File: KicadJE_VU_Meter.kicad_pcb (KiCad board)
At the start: 2 copper layers, 242 x 128 mm, 39 parts

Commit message: Update KicadJE_VU_Meter.kicad_pcb
Routed
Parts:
- removed G*** (x3): LOGO, AJ:Johansen_engineering_logo_20mm
- removed H101 (x2), H301: ON, AJ:LED_Hole_3mm
- removed H102 (x2), H103 (x2), H104, H105: MountingHole_Pad, AJ:MountingHole_Eurorack3
- removed TP102 (x2), TP303: SQ, AJ:Jack_6m3
- removed TP103 (x2), TP301: In1, AJ:Jack_6m3
- removed TP105 (x2): In3, AJ:Jack_6m3
- removed TP106 (x2): HS, AJ:Jack_6m3
- removed TP107 (x3): OFF1, AJ:Pot_6m3_scale1
- removed TP107 (x2): FM, AJ:Jack_6m3
- removed TP108 (x2): PWM, AJ:Jack_6m3
- removed TP112 (x3): Fine, AJ:Pot_6m3_scale1
- removed TP302: Tri, AJ:Jack_6m3
- removed TP304: PWM1, AJ:Pot_6m3_scale1
- removed TP305: PWM2, AJ:Pot_6m3_scale1
- added C1: 1u, Capacitor_SMD:C_0805_2012Metric, B.Cu at (136.9, 44.0)
- added C2: 1u, Capacitor_SMD:C_0805_2012Metric, B.Cu at (103.0, 45.0)
- added C4: 100n, Capacitor_SMD:C_0805_2012Metric, B.Cu at (124.5, 108.5)
- added C5: 100n, Capacitor_SMD:C_0805_2012Metric, B.Cu at (134.0, 115.5)
- added C7: 100n, Capacitor_SMD:C_0805_2012Metric, B.Cu at (130.3, 120.0)
- added C8: 220p, Capacitor_SMD:C_0805_2012Metric, B.Cu at (133.9, 118.0)
- added C9: 1u-22u, Capacitor_SMD:C_1206_3216Metric, B.Cu at (129.0, 97.0)
- added D1: 1N1007, Diode_SMD:D_SOD-123, B.Cu at (132.0, 44.0)
- added D10: 1N4148, Diode_SMD:D_MiniMELF, B.Cu at (121.5, 103.0)
- added D11: 1N4148, Diode_SMD:D_MiniMELF, B.Cu at (121.5, 97.2)
- added D2: 1N1007, Diode_SMD:D_SOD-123, B.Cu at (108.0, 45.0)
- added D3: LED, LED_SMD:LED_0805_2012Metric_Pad1.15x1.40mm_HandSolder, F.Cu at (120.4, 45.7)
- added D4: 1N1007, Diode_SMD:D_SOD-123, B.Cu at (116.5, 112.5)
- added D5: 1N1007, Diode_SMD:D_SOD-123, B.Cu at (116.5, 127.5)
- added D6: 1N1007, Diode_SMD:D_SOD-123, B.Cu at (116.5, 117.5)
- added D7: 1N1007, Diode_SMD:D_SOD-123, B.Cu at (116.5, 122.5)
- added D8: 1N4148, Diode_SMD:D_MiniMELF, B.Cu at (117.5, 103.0)
- added D9: 1N4148, Diode_SMD:D_MiniMELF, B.Cu at (117.5, 97.2)
- added H5: Meter, AJ:VU_Meter_Hole, F.Cu at (120.4, 68.6)
- added H6: Jack, AJ:Jack_6m3, F.Cu at (131.0, 145.0)
- added H7: Jack, AJ:Jack_3m5, F.Cu at (110.0, 115.0)
- added H8: Jack, AJ:Jack_3m5, F.Cu at (110.0, 125.0)
- added H9: Jack, AJ:Jack_3m5, F.Cu at (110.0, 145.0)
- added J1: Out, Connector_PinHeader_2.54mm:PinHeader_1x03_P2.54mm_Vertical_SMD_Pin1Right, B.Cu at (110.0, 153.0)
- added J2: In1, Connector_PinHeader_2.54mm:PinHeader_1x03_P2.54mm_Vertical_SMD_Pin1Right, B.Cu at (110.0, 106.0)
- added J3: In2, Connector_PinHeader_2.54mm:PinHeader_1x03_P2.54mm_Vertical_SMD_Pin1Right, B.Cu at (110.0, 134.0)
- added J4: Out, Connector_PinHeader_2.54mm:PinHeader_1x03_P2.54mm_Vertical_SMD_Pin1Right, B.Cu at (133.0, 134.0)
- added MES1: VU Meter, Connector_PinHeader_2.54mm:PinHeader_1x02_P2.54mm_Vertical_SMD_Pin1Right, B.Cu at (134.0, 97.0)
- added MES2: VU Meter Backlight, Connector_PinHeader_2.54mm:PinHeader_1x02_P2.54mm_Vertical_SMD_Pin1Right, B.Cu at (110.0, 97.0)
- added P1: HEADER_2x5_Doepfer, Connector_PinHeader_2.54mm:PinHeader_2x05_P2.54mm_Vertical_SMD, B.Cu at (121.0, 45.0)
- added R1: 22k, Resistor_SMD:R_0805_2012Metric_Pad1.20x1.40mm_HandSolder, B.Cu at (132.0, 46.5)
- added R11: 100k, Resistor_SMD:R_0805_2012Metric_Pad1.20x1.40mm_HandSolder, B.Cu at (120.5, 110.5)
- added R12: 100k, Resistor_SMD:R_0805_2012Metric_Pad1.20x1.40mm_HandSolder, B.Cu at (120.5, 113.0)
- added R13: 100k, Resistor_SMD:R_0805_2012Metric_Pad1.20x1.40mm_HandSolder, B.Cu at (126.2, 122.2)
- added R14: OPEN, Resistor_SMD:R_0805_2012Metric_Pad1.20x1.40mm_HandSolder, B.Cu at (126.2, 120.0)
- added R15: OPEN, Resistor_SMD:R_0805_2012Metric_Pad1.20x1.40mm_HandSolder, B.Cu at (120.5, 115.5)
- added R16: 100k, Resistor_SMD:R_0805_2012Metric_Pad1.20x1.40mm_HandSolder, B.Cu at (128.0, 117.5)
- added R19: 1M, Resistor_SMD:R_0805_2012Metric_Pad1.20x1.40mm_HandSolder, B.Cu at (130.2, 122.2)
- added R2: OPEN, Resistor_SMD:R_0805_2012Metric_Pad1.20x1.40mm_HandSolder, B.Cu at (103.5, 150.5)
- added R20: 10k, Resistor_SMD:R_0805_2012Metric_Pad1.20x1.40mm_HandSolder, B.Cu at (128.0, 115.5)
- added R22: 10k, Resistor_SMD:R_0805_2012Metric_Pad1.20x1.40mm_HandSolder, B.Cu at (134.2, 122.2)
- added R23: 470R, Resistor_SMD:R_0805_2012Metric_Pad1.20x1.40mm_HandSolder, B.Cu at (130.2, 124.2)
- added R24: 1k, Resistor_SMD:R_0805_2012Metric_Pad1.20x1.40mm_HandSolder, B.Cu at (124.4, 113.0)
- added R26: 150, Resistor_SMD:R_0805_2012Metric_Pad1.20x1.40mm_HandSolder, B.Cu at (125.5, 98.5)
- added R27: 150, Resistor_SMD:R_0805_2012Metric_Pad1.20x1.40mm_HandSolder, B.Cu at (125.5, 95.5)
- added R28: OPEN, Resistor_SMD:R_0805_2012Metric_Pad1.20x1.40mm_HandSolder, B.Cu at (126.0, 136.0)
- added R29: 1k, Resistor_SMD:R_0805_2012Metric_Pad1.20x1.40mm_HandSolder, B.Cu at (126.0, 131.0)
- added R3: 10k, Resistor_SMD:R_0805_2012Metric_Pad1.20x1.40mm_HandSolder, B.Cu at (103.5, 101.5)
- added R4: 10k, Resistor_SMD:R_0805_2012Metric_Pad1.20x1.40mm_HandSolder, B.Cu at (103.5, 131.5)
- added R5: 1k, Resistor_SMD:R_0805_2012Metric_Pad1.20x1.40mm_HandSolder, B.Cu at (116.5, 150.5)
- added R7: 10k, Resistor_SMD:R_0805_2012Metric_Pad1.20x1.40mm_HandSolder, B.Cu at (116.5, 108.0)
- added R8: 10k, Resistor_SMD:R_0805_2012Metric_Pad1.20x1.40mm_HandSolder, B.Cu at (116.5, 132.0)
- added TP1: Out, TestPoint:TestPoint_Pad_D2.0mm, B.Cu at (102.0, 145.0)
- added TP2: In2, TestPoint:TestPoint_Pad_D2.0mm, B.Cu at (102.0, 125.0)
- added TP3: Flow1, TestPoint:TestPoint_Pad_D2.0mm, B.Cu at (121.8, 150.2)
- added TP4: Out, TestPoint:TestPoint_Pad_D2.0mm, B.Cu at (138.0, 140.0)
- added U1: TL072, Package_SO:SO-8_5.3x6.2mm_P1.27mm, B.Cu at (131.0, 110.5)
- moved H1 93.0 mm to (106.5, 39.0)
- moved H2 93.0 mm to (106.5, 161.0)
- moved H3 93.0 mm to (133.5, 39.0)
- moved H4 93.0 mm to (133.5, 161.0)
- renumbered H102 to H1, H103 to H2, H104 to H3, H105 to H4
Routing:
- net +12VA: track 0.00 -> 216.5 mm
- net -12VA: track 0.00 -> 209.0 mm, vias 0 -> 1
- net GND: track 0.00 -> 66.3 mm, vias 0 -> 6
- net Net-(C8-Pad2): track 0.00 -> 58.6 mm, vias 0 -> 2
- net Flow1: track 0.00 -> 56.0 mm
- net Net-(C8-Pad1): track 0.00 -> 39.5 mm
- net Net-(R22-Pad1): track 0.00 -> 30.3 mm
- net Net-(D5-Pad2): track 0.00 -> 19.9 mm
- net Net-(J3-Pad1): track 0.00 -> 18.3 mm
- net Net-(J1-Pad2): track 0.00 -> 16.4 mm
- net Net-(J1-Pad1): track 0.00 -> 15.8 mm
- net Net-(J4-Pad1): track 0.00 -> 15.7 mm
- net Net-(D3-Pad2): track 0.00 -> 14.1 mm, vias 0 -> 1
- net Net-(J4-Pad2): track 0.00 -> 13.3 mm
- net Net-(D10-Pad1): track 0.00 -> 11.5 mm
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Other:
- board size 242 x 128 mm -> 40 x 128 mm
- board text added: "Johansen Engineering VU Rev A 10/04-2021"
- board text added: "Out"
- board text added: "VU"
- board text removed: "CV"
- board text removed: "CV Util Rev A 22/03-2020 Johansen Engineering"
- board text removed: "CV1"
- board text removed: "CV2"
- board text removed: "GLIDE"
- board text removed: "Gain1"
- board text removed: "Gain2"
- board text removed: "Glide1"
- board text removed: "Glide2"
- board text removed: "IN"
- board text removed: "Inv1"
- board text removed: "Inv2"
- board text removed: "Johansen Engineering Glide Rev A 22/03-2020"
- board text removed: "Offset1"
- board text removed: "Offset2"
- board text removed: "Out1"
- board text removed: "Out2"
- board text removed: "Phase1"
- board text removed: "Phase2"
- board text removed: "SHIFT"
- board text removed: "TIME"
- board text removed: "TimeShift Rev A 22/03-2020 Johansen Engineering"

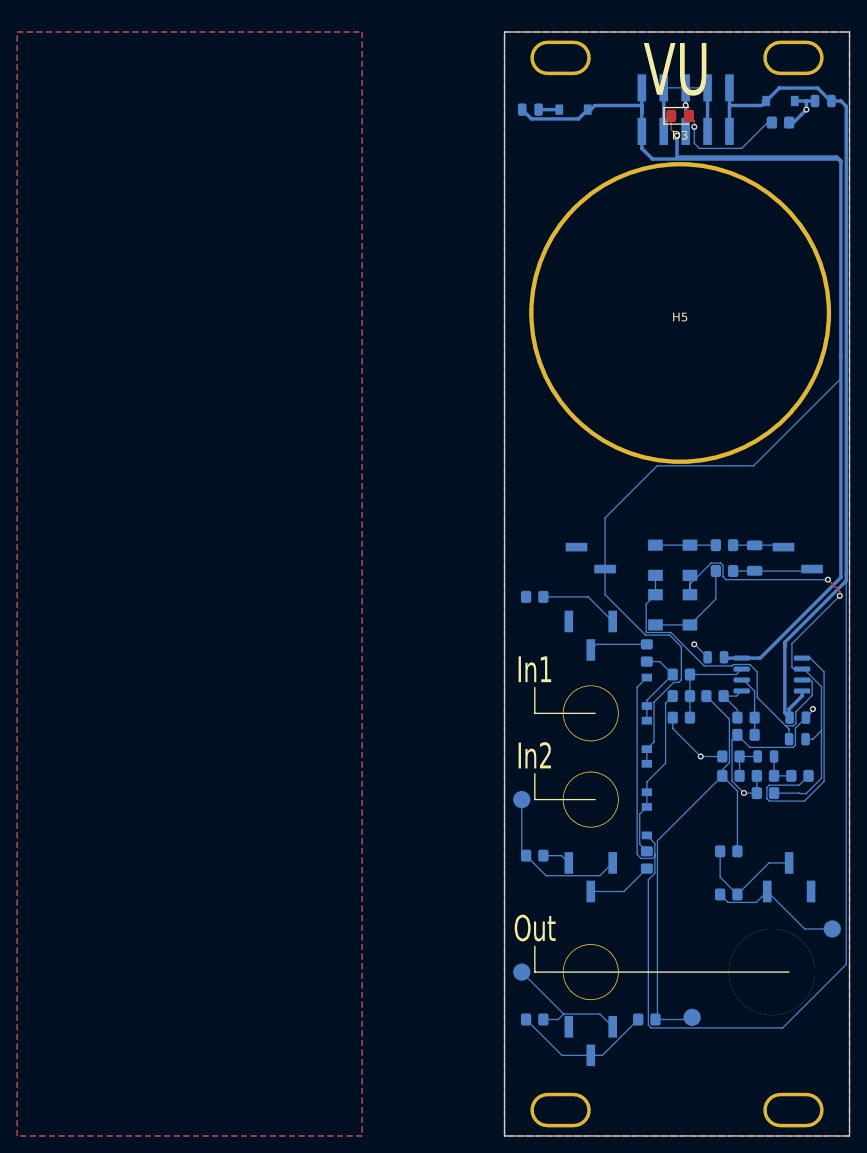
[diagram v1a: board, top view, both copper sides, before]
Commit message: Reposition VU meter
To make sure there is room for the power conn.
2mm available for jacks
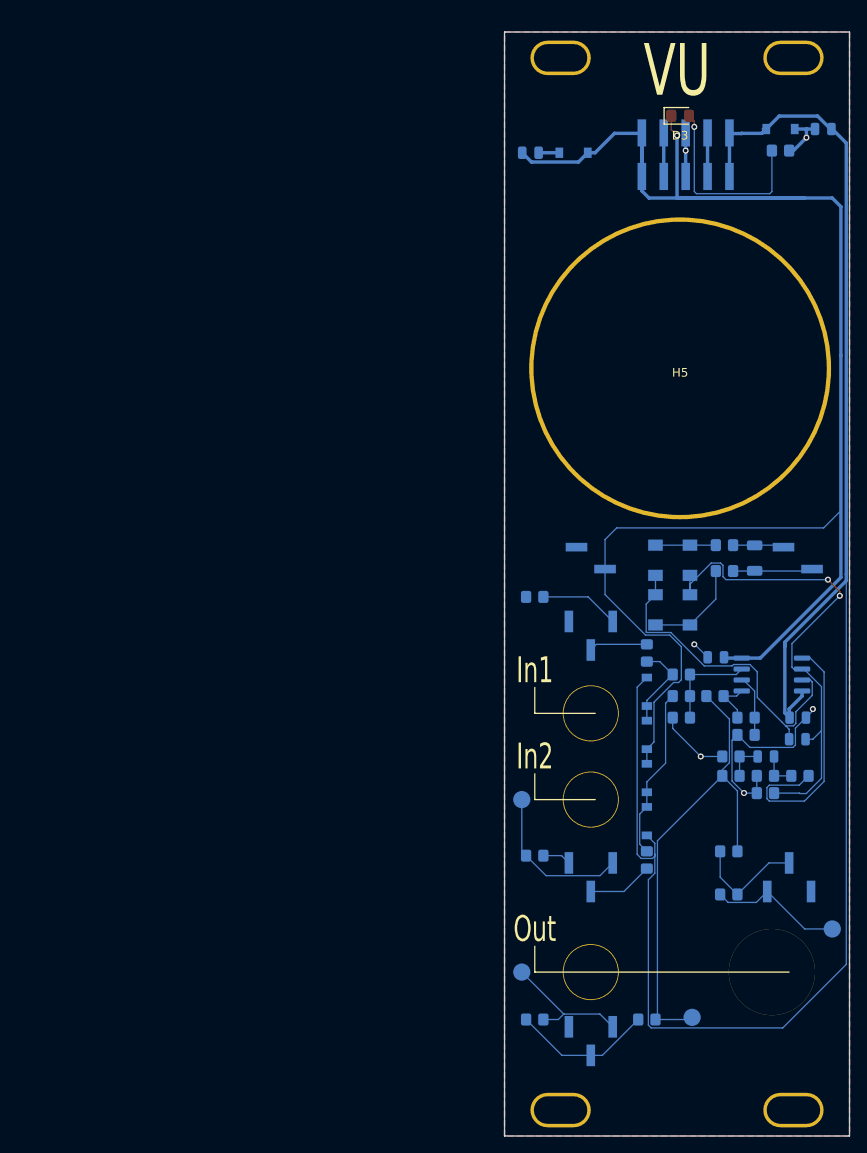
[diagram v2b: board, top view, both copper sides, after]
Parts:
- moved H5 6.42 mm to (120.4, 75.0)
- moved P1 5.23 mm to (121.0, 50.2)
- moved C2 5.00 mm to (103.0, 50.0)
- moved D2 5.00 mm to (108.0, 50.0)
- moved C1 3.25 mm to (136.9, 47.2)
- moved D1 3.25 mm to (132.0, 47.2)
- moved R1 3.25 mm to (132.0, 49.8)
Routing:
- net Net-(D3-Pad2): track 14.1 -> 22.7 mm
- net -12VA: track 209.0 -> 217.6 mm
- net GND: track 66.3 -> 61.2 mm
- net +12VA: track 216.5 -> 212.9 mm

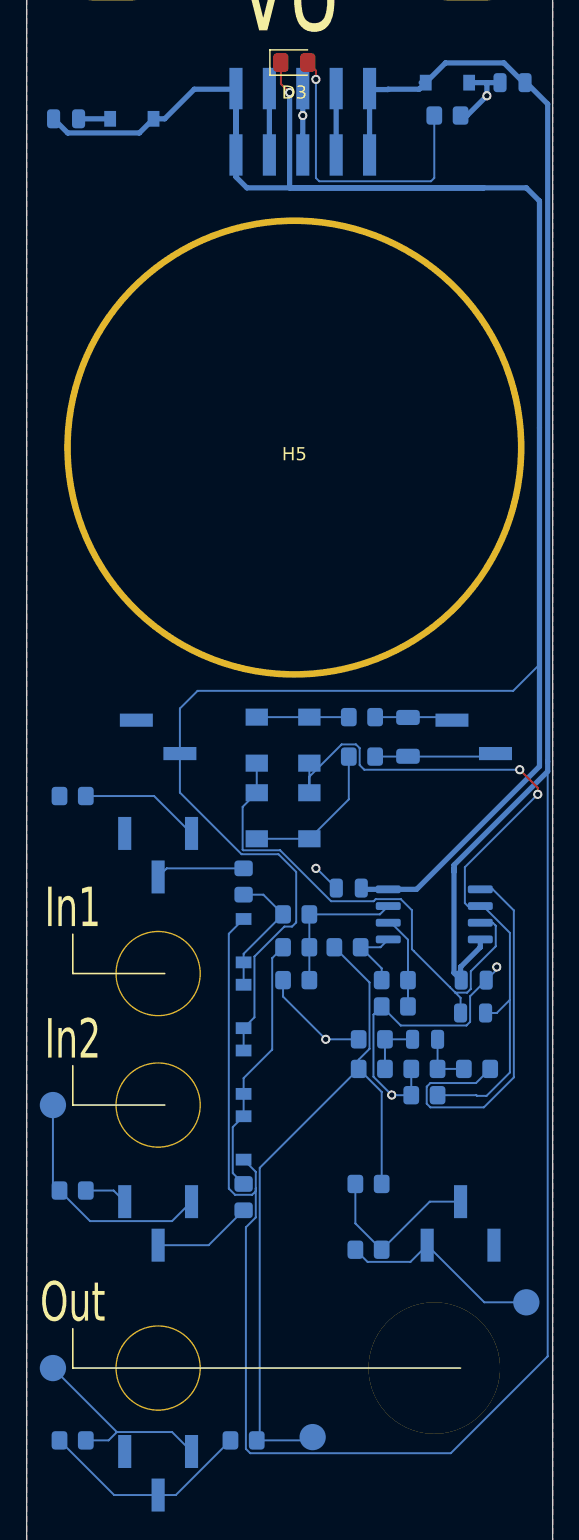
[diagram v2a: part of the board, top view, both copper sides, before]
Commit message: Adjusting labels
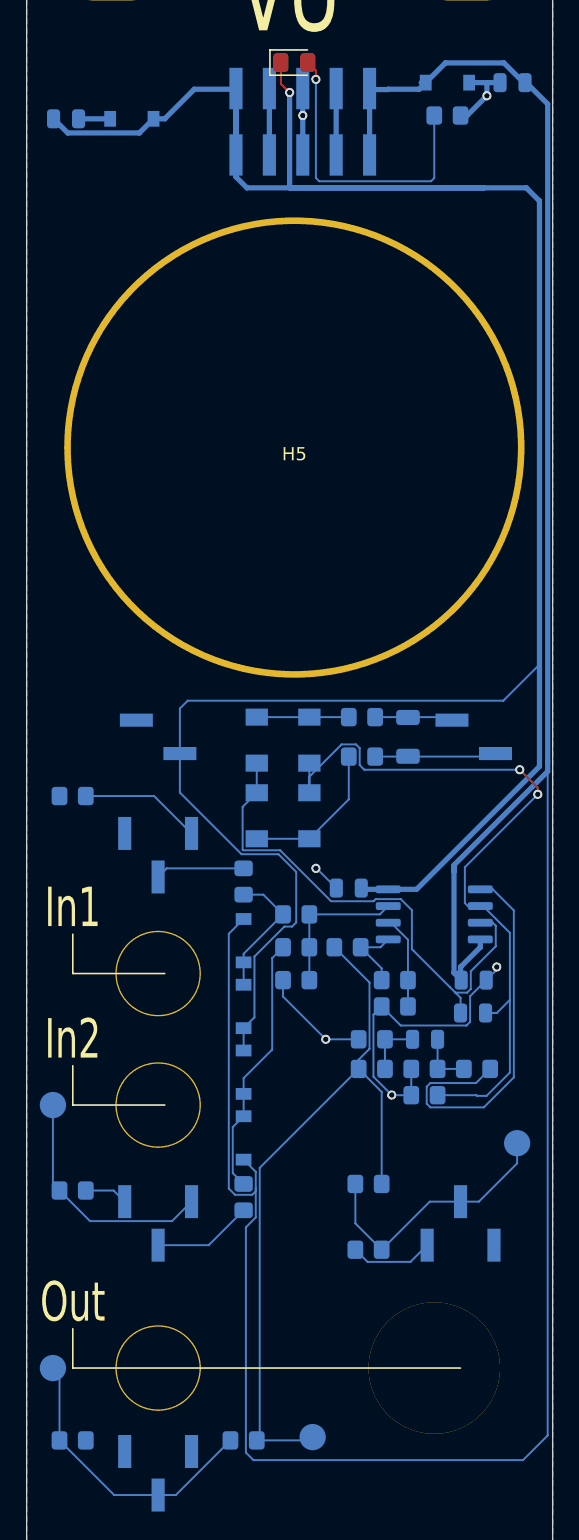
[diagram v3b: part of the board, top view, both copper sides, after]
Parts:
- moved TP4 12.1 mm to (137.3, 127.9)
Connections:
- J1 pad 1: Net-(J1-Pad1) -> GND
- J4 pad 1: Net-(J4-Pad1) -> GND
- R2 pad 1: Net-(J1-Pad1) -> GND
- R28 pad 1: Net-(J4-Pad1) -> GND
- TP1 pad 1: Net-(J1-Pad1) -> Net-(J1-Pad2)
- TP4 pad 1: Net-(J4-Pad1) -> Net-(J4-Pad2)
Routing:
- net Net-(J1-Pad1): track 15.8 -> 0.00 mm
- net Net-(J4-Pad1): track 15.7 -> 0.00 mm
- net Net-(J4-Pad2): track 13.3 -> 20.4 mm
- net GND: track 61.2 -> 67.6 mm
- net Net-(J1-Pad2): track 16.4 -> 22.1 mm
- net +12VA: track 212.9 -> 217.0 mm
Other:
- board text added: "-12v"
- board text added: "GND"
- board text added: "NEG"
- board text added: "POS"

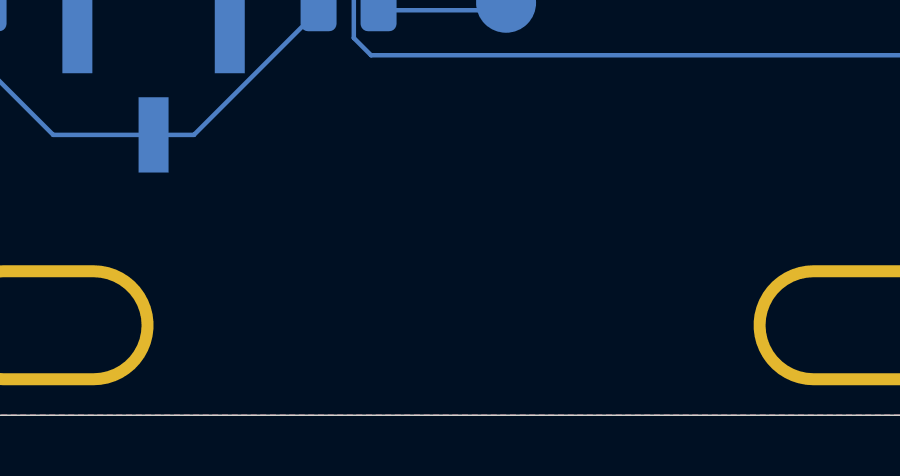
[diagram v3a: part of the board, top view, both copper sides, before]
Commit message: Faceplate cleanup
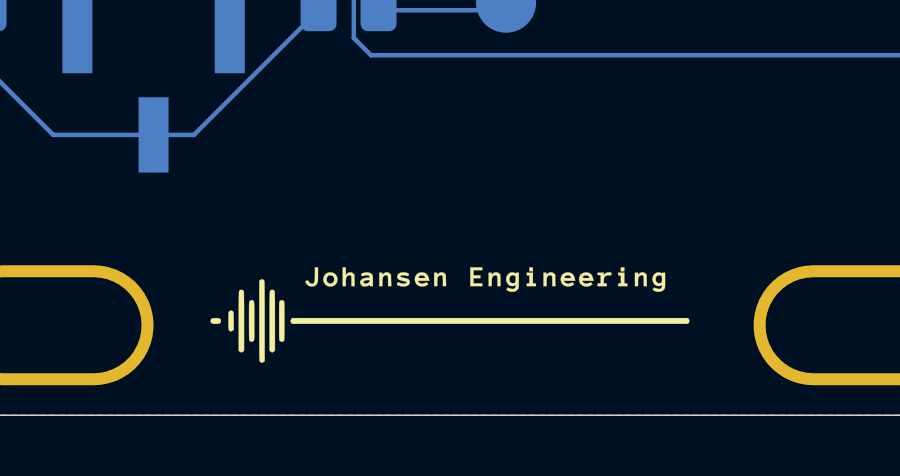
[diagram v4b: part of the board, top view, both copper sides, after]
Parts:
- added G***: LOGO, AJ:Johansen_engineering_logo_20mm, F.Cu at (119.9, 160.8)
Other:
- board text added: "+"
- board text added: "+12v"
- board text added: "SW"
- board text added: "Signal"

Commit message: Gerber
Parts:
- moved C1 4.80 mm to (136.9, 52.0)
- moved D1 4.80 mm to (132.0, 52.0)
- moved R1 2.70 mm to (133.5, 47.5)
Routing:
- net -12VA: track 217.6 -> 195.5 mm
- net GND: track 67.6 -> 77.8 mm, vias 6 -> 5
- net Net-(D3-Pad2): track 22.7 -> 16.1 mm
- net +12VA: track 217.0 -> 211.7 mm
